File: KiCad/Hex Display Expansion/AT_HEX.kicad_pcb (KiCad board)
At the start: 2 copper layers, 101.1 x 77.4 mm, 38 parts, among them J1 Expansion Connector, J2 PWR, Q1 BC557, Q2 BC557, Q3 BC557, Q4 BC557, Q5 BC557, Q6 BC557, U1 NE555P, U10 HDSP-7801, U11 HDSP-7801, U12 HDSP-7801, U13 74HC244, U14 74HC244, U2 GAL16V8, U3 HDSP-7801, U4 HDSP-7801, U5 74HC74, U6 74HC00, U7 74HC04, U8 GAL16V8, U9 HDSP-7801

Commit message: Hex Display Updates WIP
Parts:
- removed the REF** at (111.7, 63.6)
- moved REF** 42.8 mm to (163.7, 112.2)
- moved REF** 17.3 mm to (157.3, 71.2), turned to 180 degrees
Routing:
- net /~Q0: track 26.6 -> 49.4 mm, vias 0 -> 1
- net /Q1: track 18.4 -> 31.6 mm, vias 0 -> 1
- net EN_H: track 110.7 -> 112.7 mm
- net HEX2: track 106.4 -> 107.8 mm
- net (no net): vias 1 -> 0
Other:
- board text added: "AT65C02 Hex Display"
- board text added: "https://github.com/Kayto"
- board text removed: "+3.3V"
- board text removed: "+5V"
- board text removed: "65C02 Hobby Computer - AT65C02"
- board text removed: "A00"
- board text removed: "A01"
- board text removed: "A02"
- board text removed: "A03"
- board text removed: "A04"
- board text removed: "A05"
- board text removed: "A06"
- board text removed: "A07"
- board text removed: "A08"
- board text removed: "A09"
- board text removed: "A10"
- board text removed: "A11"
- board text removed: "A12"
- board text removed: "A13"
- board text removed: "A14"
- board text removed: "A15"
- board text removed: "Based on Ben Eater’s 6502 project and"
- board text removed: "CLK"
- board text removed: "D0"
- board text removed: "D1"
- board text removed: "D2"
- board text removed: "D3"
- board text removed: "D4"
- board text removed: "D5"
- board text removed: "D6"
- board text removed: "D7"
- board text removed: "GND"
- board text removed: "NC"
- board text removed: "R~W"
- board text removed: "SIGNAL"
- board text removed: "https://github.com/dbuchwald/6502"
- board text removed: "the PCB designs by Dawid Buchwald"
- board text removed: "~IOCS"
- board text removed: "~IRQ"
- board text removed: "~RES"
- board text removed: "~ROMCS"
- board text removed: "~ROMOE"

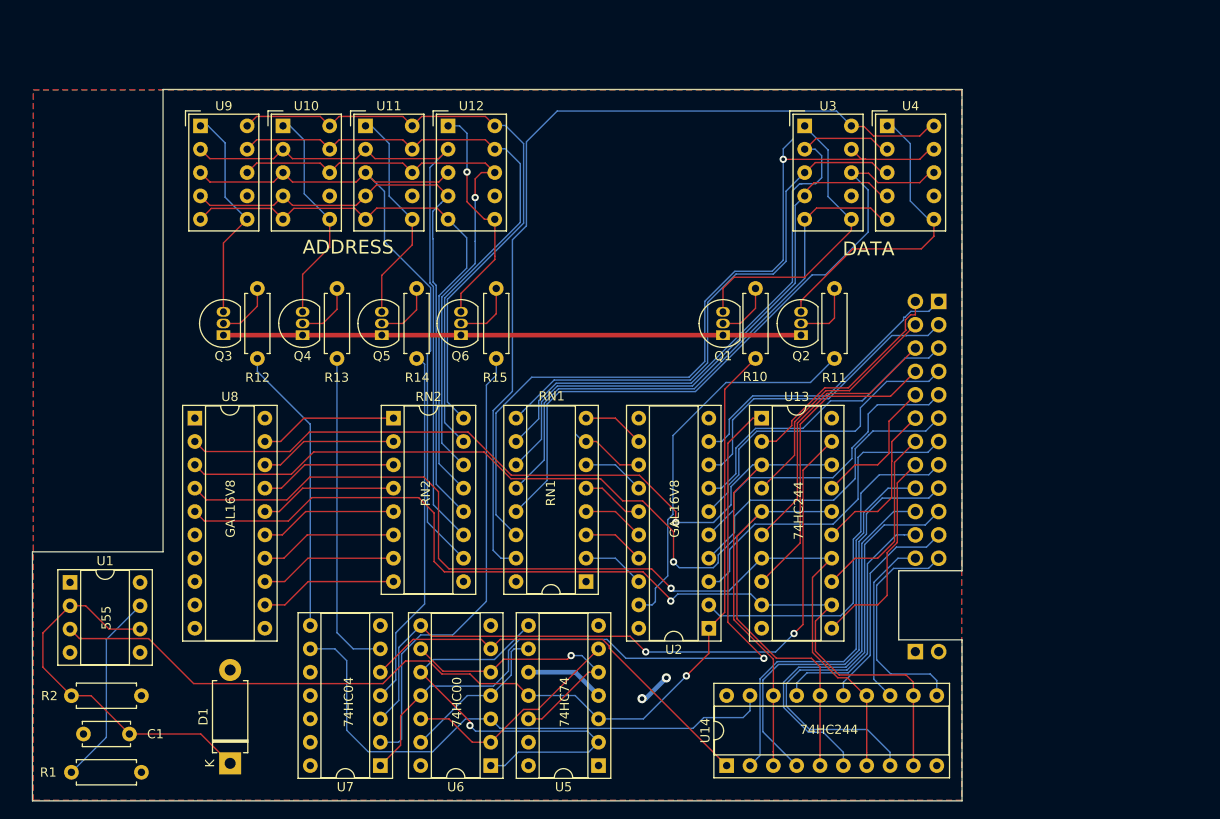
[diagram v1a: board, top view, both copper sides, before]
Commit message: HEX Board Mods
Hex board changes. Main board Hex to Latches
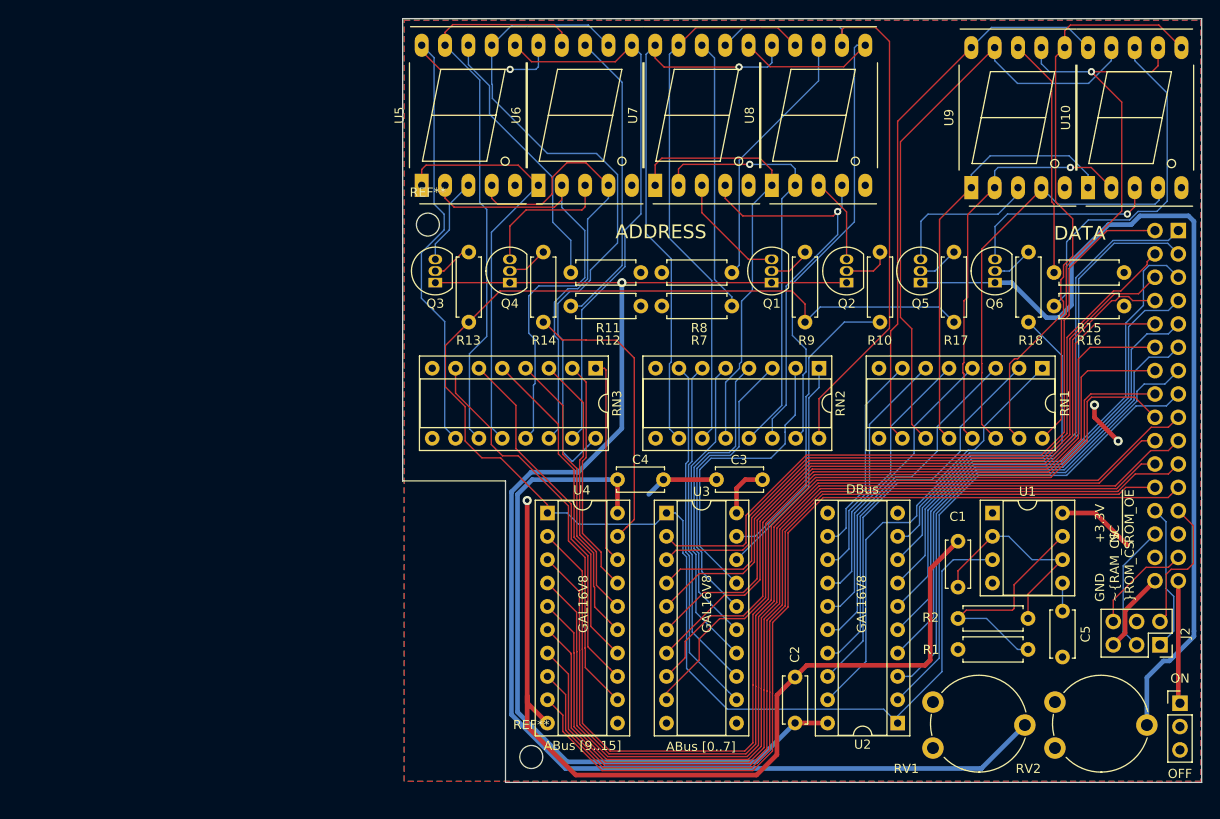
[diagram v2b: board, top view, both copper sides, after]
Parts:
- removed D1: D, Diode_THT:D_DO-15_P10.16mm_Horizontal
- removed U11, U12: HDSP-7801, Display_7Segment:HDSP-7801
- removed U13, U14: 74HC244, Package_DIP:DIP-20_W7.62mm_Socket
- added C2: 100n, Capacitor_THT:C_Disc_D5.0mm_W2.5mm_P5.00mm, F.Cu at (177.6, 113.5)
- added C3: 100n, Capacitor_THT:C_Disc_D5.0mm_W2.5mm_P5.00mm, F.Cu at (174.0, 87.0)
- added C4: 100n, Capacitor_THT:C_Disc_D5.0mm_W2.5mm_P5.00mm, F.Cu at (158.2, 87.0)
- added C5: 0.01uF, Capacitor_THT:C_Disc_D5.0mm_W2.5mm_P5.00mm, F.Cu at (206.7, 101.3)
- added J3: Conn_01x03, Connector_PinHeader_2.54mm:PinHeader_1x03_P2.54mm_Vertical, F.Cu at (219.4, 111.4)
- added R16: 2k2, Resistor_THT:R_Axial_DIN0207_L6.3mm_D2.5mm_P7.62mm_Horizontal, F.Cu at (205.7, 68.2)
- added R17: 4k7, Resistor_THT:R_Axial_DIN0207_L6.3mm_D2.5mm_P7.62mm_Horizontal, F.Cu at (194.9, 62.3)
- added R18: 2k2, Resistor_THT:R_Axial_DIN0207_L6.3mm_D2.5mm_P7.62mm_Horizontal, F.Cu at (203.0, 62.3)
- added R7: 4k7, Resistor_THT:R_Axial_DIN0207_L6.3mm_D2.5mm_P7.62mm_Horizontal, F.Cu at (163.1, 68.2)
- added R8: 4k7, Resistor_THT:R_Axial_DIN0207_L6.3mm_D2.5mm_P7.62mm_Horizontal, F.Cu at (163.1, 64.5)
- added R9: 4k7, Resistor_THT:R_Axial_DIN0207_L6.3mm_D2.5mm_P7.62mm_Horizontal, F.Cu at (178.6, 62.3)
- added REF**: MountingHole_2.5mm, MountingHole:MountingHole_2.5mm, F.Cu at (148.9, 117.2)
- added REF**: MountingHole_2.5mm, MountingHole:MountingHole_2.5mm, F.Cu at (137.6, 59.3)
- added RN3: 100, Package_DIP:DIP-16_W7.62mm_Socket, F.Cu at (155.9, 74.9)
- added RV1: R_POT_Small, Potentiometer_THT:Potentiometer_Piher_PT-10-V10_Vertical, F.Cu at (192.6, 116.2)
- added RV2: R_POT_Small, Potentiometer_THT:Potentiometer_Piher_PT-10-V10_Vertical, F.Cu at (205.8, 116.2)
- C1: value 68n -> 0.01uF
- J1: footprint Connector_PinHeader_2.54mm:PinHeader_2x12_P2.54mm_Vertical -> Connector_PinHeader_2.54mm:PinHeader_2x16_P2.54mm_Vertical
- J2: value PWR -> Conn_02x03_Odd_Even; footprint Connector_PinHeader_2.54mm:PinHeader_1x02_P2.54mm_Vertical -> Connector_PinSocket_2.54mm:PinSocket_2x03_P2.54mm_Vertical; moved to F.Cu
- R1: value 51k -> 1k
- R11, R12, R13, R14: value 2k2 -> 4k7
- R2: value 51k -> 100k
- U10, U9: value HDSP-7801 -> E10561; footprint Display_7Segment:HDSP-7801 -> Display_7Segment:7SegmentLED_LTS6760_LTS6780
- U3, U4: value HDSP-7801 -> GAL16V8; footprint Display_7Segment:HDSP-7801 -> Package_DIP:DIP-20_W7.62mm_Socket
- U5: value 74HC74 -> E10561; footprint Package_DIP:DIP-14_W7.62mm_Socket -> Display_7Segment:7SegmentLED_LTS6760_LTS6780
- U6: value 74HC00 -> E10561; footprint Package_DIP:DIP-14_W7.62mm_Socket -> Display_7Segment:7SegmentLED_LTS6760_LTS6780
- U7: value 74HC04 -> E10561; footprint Package_DIP:DIP-14_W7.62mm_Socket -> Display_7Segment:7SegmentLED_LTS6760_LTS6780
- U8: value GAL16V8 -> E10561; footprint Package_DIP:DIP-20_W7.62mm_Socket -> Display_7Segment:7SegmentLED_LTS6760_LTS6780
- moved U1 100.6 mm to (199.0, 90.7)
- moved C1 91.6 mm to (195.3, 98.8), turned to 90 degrees
- moved R1 89.8 mm to (195.3, 105.5), turned to 0 degrees
- moved R2 89.2 mm to (195.3, 102.2), turned to 0 degrees
- moved U10 87.8 mm to (209.4, 55.3), turned to 90 degrees
- moved U9 84.1 mm to (196.7, 55.3), turned to 90 degrees
- moved REF** 71.3 mm to (191.0, 46.3)
- moved U7 69.9 mm to (162.3, 55.0), turned to 90 degrees
- moved U8 67.7 mm to (175.0, 55.0), turned to 90 degrees
- moved U5 66.0 mm to (136.9, 55.0), turned to 90 degrees
- moved U6 63.3 mm to (149.6, 55.0), turned to 90 degrees
- moved R15 60.7 mm to (205.7, 64.5), turned to 0 degrees
- moved Q5 58.9 mm to (191.2, 65.6)
- moved Q6 58.4 mm to (199.3, 65.6)
- moved U4 56.0 mm to (150.6, 90.7)
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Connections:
- J2 pad 1: +5V -> ~ROM_CS
- J2 pad 2: GND -> ~ROM_OE
- Q1 pad 1: +5V -> Net-(Q1-Pad1)
- Q2 pad 1: +5V -> Net-(Q1-Pad1)
- Q3 pad 1: +5V -> Net-(Q1-Pad1)
- Q4 pad 1: +5V -> Net-(Q1-Pad1)
- Q5 pad 1: +5V -> Net-(Q5-Pad1)
- Q6 pad 1: +5V -> Net-(Q5-Pad1)
- R10 pad 1: Net-(Q1-Pad2) -> Net-(Q2-Pad2)
- R10 pad 2: EN_H -> EN_a0L
- R11 pad 1: Net-(Q2-Pad2) -> GND
- R11 pad 2: EN_D0 -> Net-(R11-Pad2)
- R12 pad 1: Net-(Q3-Pad2) -> GND
- R13 pad 1: Net-(Q4-Pad2) -> Net-(Q3-Pad2)
- R13 pad 2: Net-(R13-Pad2) -> EN_H
- R14 pad 1: Net-(Q5-Pad2) -> Net-(Q4-Pad2)
- R14 pad 2: Net-(R14-Pad2) -> EN_a8L
- R15 pad 1: Net-(Q6-Pad2) -> Net-(R15-Pad1)
- R15 pad 2: Net-(R15-Pad2) -> GND
- R2 pad 1: +5V -> Net-(R1-Pad2)
- RN2 pad 10: /16 bit Hex/G -> Net-(RN2-Pad10)
- RN2 pad 11: /16 bit Hex/F -> Net-(RN2-Pad11)
- RN2 pad 12: /16 bit Hex/E -> Net-(RN2-Pad12)
- RN2 pad 13: /16 bit Hex/D -> Net-(RN2-Pad13)
- RN2 pad 14: /16 bit Hex/C -> Net-(RN2-Pad14)
- RN2 pad 15: /16 bit Hex/B -> Net-(RN2-Pad15)
- RN2 pad 16: /16 bit Hex/A -> Net-(RN2-Pad16)
- U1 pad 4: +5V -> Net-(U1-Pad4)
- U10 pad 1: Net-(Q4-Pad3) -> Net-(RN1-Pad12)
- U10 pad 10: /16 bit Hex/A -> Net-(RN1-Pad10)
- U10 pad 2: /16 bit Hex/F -> Net-(RN1-Pad13)
- U10 pad 3: /16 bit Hex/G -> Net-(Q6-Pad3)
- U10 pad 4: /16 bit Hex/E -> Net-(RN1-Pad14)
- U10 pad 5: /16 bit Hex/D -> Net-(U10-Pad5)
- U10 pad 6: Net-(Q4-Pad3) -> Net-(RN1-Pad15)
- U10 pad 7: Net-(U10-Pad7) -> Net-(RN1-Pad16)
- U10 pad 8: /16 bit Hex/C -> Net-(R16-Pad1)
- U10 pad 9: /16 bit Hex/B -> Net-(RN1-Pad11)
- U2 pad 10: GND -> Net-(U2-Pad10)
- U2 pad 12: Net-(RN1-Pad8) -> Net-(RN1-Pad7)
- U2 pad 13: Net-(RN1-Pad7) -> Net-(RN1-Pad6)
- U2 pad 14: Net-(RN1-Pad6) -> Net-(RN1-Pad5)
- U2 pad 15: Net-(RN1-Pad5) -> Net-(RN1-Pad4)
- U2 pad 16: Net-(RN1-Pad4) -> Net-(RN1-Pad3)
- U2 pad 17: Net-(RN1-Pad3) -> Net-(RN1-Pad2)
- U2 pad 18: Net-(RN1-Pad2) -> Net-(RN1-Pad1)
- U2 pad 19: EN_D0 -> EN_DL
- U3 pad 1: Net-(Q1-Pad3) -> EN_H
- U3 pad 10: Net-(RN1-Pad15) -> GND
- U3 pad 2: Net-(RN1-Pad10) -> a0
- U3 pad 3: Net-(RN1-Pad9) -> a1
- U3 pad 4: Net-(RN1-Pad11) -> a2
- U3 pad 5: Net-(RN1-Pad12) -> a3
- U3 pad 6: Net-(Q1-Pad3) -> a4
- U3 pad 7: Net-(U3-Pad7) -> a5
- U3 pad 8: Net-(RN1-Pad13) -> a6
- U3 pad 9: Net-(RN1-Pad14) -> a7
- U4 pad 1: Net-(Q2-Pad3) -> EN_H
- U4 pad 10: Net-(RN1-Pad15) -> GND
- U4 pad 2: Net-(RN1-Pad10) -> a8
- U4 pad 3: Net-(RN1-Pad9) -> a9
- U4 pad 4: Net-(RN1-Pad11) -> a10
- U4 pad 5: Net-(RN1-Pad12) -> a11
- U4 pad 6: Net-(Q2-Pad3) -> a12
- U4 pad 7: Net-(U4-Pad7) -> a13
- U4 pad 8: Net-(RN1-Pad13) -> a14
- U4 pad 9: Net-(RN1-Pad14) -> a15
- U5 pad 1: +5V -> Net-(RN3-Pad12)
- U5 pad 10: +5V -> Net-(RN3-Pad10)
- U5 pad 2: /~Q0 -> Net-(RN3-Pad13)
- U5 pad 3: EN_H -> Net-(Q3-Pad3)
- U5 pad 4: +5V -> Net-(RN3-Pad14)
- U5 pad 5: /Q1 -> Net-(U5-Pad5)
- U5 pad 6: /~Q1 -> Net-(RN3-Pad15)
- U5 pad 7: GND -> Net-(RN3-Pad16)
- U5 pad 8: /~Q0 -> Net-(R11-Pad2)
- U5 pad 9: /Q0 -> Net-(RN3-Pad11)
- U6 pad 1: /~Q0 -> Net-(RN3-Pad12)
- U6 pad 10: /~Q0 -> Net-(RN3-Pad10)
- U6 pad 2: /~Q1 -> Net-(RN3-Pad13)
- U6 pad 3: EN_DIG0 -> Net-(Q4-Pad3)
- U6 pad 4: /Q0 -> Net-(RN3-Pad14)
- U6 pad 5: /Q1 -> Net-(U6-Pad5)
- U6 pad 6: EN_DIG1 -> Net-(RN3-Pad15)
- U6 pad 7: GND -> Net-(RN3-Pad16)
- U6 pad 8: EN_DIG2 -> Net-(R12-Pad2)
- U6 pad 9: /Q1 -> Net-(RN3-Pad11)
- U7 pad 1: EN_DIG3 -> Net-(RN2-Pad12)
- U7 pad 10: (no net) -> Net-(RN2-Pad10)
- U7 pad 2: Net-(R15-Pad2) -> Net-(RN2-Pad13)
- U7 pad 3: EN_DIG2 -> Net-(Q1-Pad3)
- U7 pad 4: Net-(R14-Pad2) -> Net-(RN2-Pad14)
- U7 pad 5: EN_DIG1 -> Net-(U7-Pad5)
- U7 pad 6: Net-(R13-Pad2) -> Net-(RN2-Pad15)
- U7 pad 7: GND -> Net-(RN2-Pad16)
- U7 pad 8: Net-(R12-Pad2) -> Net-(R7-Pad2)
- U7 pad 9: EN_DIG0 -> Net-(RN2-Pad11)
- U8 pad 1: Net-(U8-Pad1) -> Net-(RN2-Pad12)
- U8 pad 10: GND -> Net-(RN2-Pad10)
- U8 pad 2: HEX0 -> Net-(RN2-Pad13)
- U8 pad 3: HEX1 -> Net-(Q2-Pad3)
- U8 pad 4: HEX2 -> Net-(RN2-Pad14)
- U8 pad 5: HEX3 -> Net-(U8-Pad5)
- U8 pad 6: Net-(U8-Pad6) -> Net-(RN2-Pad15)
- U8 pad 7: Net-(U8-Pad7) -> Net-(RN2-Pad16)
- U8 pad 9: Net-(U8-Pad9) -> Net-(RN2-Pad11)
- U9 pad 1: Net-(Q3-Pad3) -> Net-(RN1-Pad12)
- U9 pad 10: /16 bit Hex/A -> Net-(RN1-Pad10)
- U9 pad 2: /16 bit Hex/F -> Net-(RN1-Pad13)
- U9 pad 3: /16 bit Hex/G -> Net-(Q5-Pad3)
- U9 pad 4: /16 bit Hex/E -> Net-(RN1-Pad14)
- U9 pad 5: /16 bit Hex/D -> Net-(U9-Pad5)
- U9 pad 6: Net-(Q3-Pad3) -> Net-(RN1-Pad15)
- U9 pad 7: Net-(U9-Pad7) -> Net-(RN1-Pad16)
- U9 pad 8: /16 bit Hex/C -> Net-(R15-Pad1)
- U9 pad 9: /16 bit Hex/B -> Net-(RN1-Pad11)
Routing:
- net Net-(Q1-Pad1): track 0.00 -> 160.0 mm, vias 0 -> 1
- net GND: track 0.00 -> 120.0 mm, vias 0 -> 3
- net HEX1: track 115.2 -> 0.00 mm, vias 1 -> 0
- net HEX0: track 115.0 -> 0.00 mm, vias 1 -> 0
- net HEX2: track 107.8 -> 0.00 mm, vias 1 -> 0
- net HEX3: track 106.3 -> 0.00 mm, vias 1 -> 0
- net Net-(Q5-Pad1): track 0.00 -> 96.2 mm
- net EN_DIG3: track 81.4 -> 0.00 mm, vias 1 -> 0
- net a13: track 23.7 -> 103.7 mm
- net a14: track 18.6 -> 98.1 mm
- net EN_DIG2: track 77.2 -> 0.00 mm, vias 2 -> 0
- net a12: track 26.7 -> 103.2 mm
- net /16 bit Hex/G: track 76.2 -> 0.00 mm
- net Net-(RN3-Pad16): track 0.00 -> 76.1 mm
- net a8: track 43.6 -> 117.8 mm
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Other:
- board size 101.1 x 77.4 mm -> 86.9 x 83.1 mm
- board text added: "+3.3V NC ~ROM_OE"
- board text added: "ABus [0..7]"
- board text added: "ABus [9..15]"
- board text added: "DBus"
- board text added: "GND ~RAM_CS ~ROM_CS"
- board text added: "OFF"
- board text added: "ON"
- board text removed: "555"
- board text removed: "74HC00"
- board text removed: "74HC04"
- board text removed: "74HC244"
- board text removed: "74HC74"
- board text removed: "RN1"
- board text removed: "RN2"
- board text removed: "https://github.com/kayto/AT65C02"

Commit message: release revisions
REv001,002 and HEX
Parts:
- REF**: value MountingHole_2.5mm -> MountingHole_2.1mm; footprint MountingHole:MountingHole_2.5mm -> MountingHole:MountingHole_2.1mm
- moved REF** 17.3 mm to (160.9, 104.8)
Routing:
- net GND: track 120.0 -> 124.2 mm
- net +5V: track 91.1 -> 92.8 mm
- net Net-(Q1-Pad1): track 160.0 -> 161.8 mm
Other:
- board text added: "+3.3V NC ~ROMOE"
- board text added: "ABus [8..15]"
- board text added: "GND ~RAMCS ~ROMCS"
- board text removed: "+3.3V NC ~ROM_OE"
- board text removed: "ABus [9..15]"
- board text removed: "GND ~RAM_CS ~ROM_CS"
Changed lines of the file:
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@@
     (thickness 1.6)
     (drawings 23)
-    (tracks 991)
+    (tracks 993)
     (zones 0)
     (modules 48)
@@
   (page A4)
   (layers
-    (0 F.Cu signal)
-    (31 B.Cu signal)
+    (0 F.Cu signal hide)
+    (31 B.Cu signal hide)
     (32 B.Adhes user)
     (33 F.Adhes user)
     (34 B.Paste user)
     (35 F.Paste user)
-    (36 B.SilkS user hide)
+    (36 B.SilkS user)
     (37 F.SilkS user)
     (38 B.Mask user)
@@
   )
   (setup
-    (last_trace_width 0.508)
+    (last_trace_width 0.1524)
     (user_trace_width 0.25)
     (user_trace_width 0.25)
@@
       (drillshape 0)
       (scaleselection 1)
-      (outputdirectory "Gerbers/AT_65c02/"))
+      (outputdirectory "../../Gerbers/Hex Rev001/"))
   )
   (net 0 "")
@@
     (add_net GND)
   )
-  (module MountingHole:MountingHole_2.5mm (layer F.Cu)
-    (at 148.865 117.225)
-    (descr "Mounting Hole 2.5mm, no annular")
-    (tags "mounting hole 2.5mm no annular")
+  (module MountingHole:MountingHole_2.1mm (layer F.Cu)
+    (at 160.89 104.775)
+    (descr "Mounting Hole 2.1mm, no annular")
+    (tags "mounting hole 2.1mm no annular")
     (attr virtual)
-    (fp_text reference REF** (at 0 -3.5) (layer F.SilkS)
+    (fp_text reference REF** (at 0 -3.5) (layer F.SilkS) hide
       (effects (font (size 1 1) (thickness 0.15)))
     )
-    (fp_text value MountingHole_2.5mm (at 0 3.5) (layer F.Fab)
+    (fp_text value MountingHole_2.1mm (at 0 3.5) (layer F.Fab)
       (effects (font (size 1 1) (thickness 0.15)))
     )
-    (fp_circle (center 0 0) (end 2.75 0) (layer F.CrtYd) (width 0.05))
-    (fp_circle (center 0 0) (end 2.5 0) (layer Cmts.User) (width 0.15))
+    (fp_circle (center 0 0) (end 2.35 0) (layer F.CrtYd) (width 0.05))
+    (fp_circle (center 0 0) (end 2.1 0) (layer Cmts.User) (width 0.15))
     (fp_text user %R (at 0.3 0) (layer F.Fab)
       (effects (font (size 1 1) (thickness 0.15)))
     )
-    (pad 1 np_thru_hole circle (at 0 0) (size 2.5 2.5) (drill 2.5) (layers *.Cu *.Mask))
+    (pad "" np_thru_hole circle (at 0 0) (size 2.1 2.1) (drill 2.1) (layers *.Cu *.Mask))
   )
   (module MountingHole:MountingHole_2.5mm (layer F.Cu)
@@
     (tags "mounting hole 2.5mm no annular")
     (attr virtual)
-    (fp_text reference REF** (at 0 -3.5) (layer F.SilkS)
+    (fp_text reference REF** (at 0 -3.5) (layer F.SilkS) hide
       (effects (font (size 1 1) (thickness 0.15)))
     )
@@
     (descr "7-Segment Display, LTS67x0, http://optoelectronics.liteon.com/upload/download/DS30-2001-355/S6760jd.pdf")
     (tags "7Segment LED LTS6760 LTS6780")
-    (fp_text reference U5 (at 7.62 -2.42 90) (layer F.SilkS)
+    (fp_text reference U5 (at 7.903 -0.225 90) (layer F.SilkS)
       (effects (font (size 1 1) (thickness 0.15)))
     )
@@
       (effects (font (size 1 1) (thickness 0.15)))
     )
-    (fp_text user %R (at 0 2.54 90) (layer F.Fab)
-      (effects (font (size 1 1) (thickness 0.15)))
-    )
     (fp_line (start -0.635 -1.27) (end 1.27 -1.27) (layer F.Fab) (width 0.1))
     (fp_line (start 1.27 -1.27) (end 1.27 6.35) (layer F.Fab) (width 0.1))
@@
     (fp_line (start 1.8 6.85) (end 1.8 -1.8) (layer F.CrtYd) (width 0.05))
     (fp_line (start 1.8 -1.8) (end -1.8 -1.8) (layer F.CrtYd) (width 0.05))
+    (fp_text user %R (at 0 2.54 90) (layer F.Fab)
+      (effects (font (size 1 1) (thickness 0.15)))
+    )
     (pad 3 thru_hole oval (at 0 5.08) (size 1.7 1.7) (drill 1) (layers *.Cu *.Mask)
       (net 122 "Net-(J3-Pad3)"))
@@
     (effects (font (size 1 1) (thickness 0.15)))
   )
-  (gr_text "GND\n~RAM_CS\n~ROM_CS" (at 212.34 100.35 90) (layer F.SilkS)
+  (gr_text "GND\n~RAMCS\n~ROMCS" (at 212.34 100.35 90) (layer F.SilkS)
     (effects (font (size 1 1) (thickness 0.15)) (justify left))
   )
@@
     (effects (font (size 1 1) (thickness 0.15)))
   )
-  (gr_text "ABus [9..15]" (at 154.44 116) (layer F.SilkS)
+  (gr_text "ABus [8..15]" (at 154.44 116) (layer F.SilkS)
     (effects (font (size 1 1) (thickness 0.15)))
   )
@@
     (effects (font (size 1 1) (thickness 0.15)))
   )
-  (gr_text "+3.3V\nNC\n~ROM_OE" (at 212.34 93.95 90) (layer F.SilkS)
+  (gr_text "+3.3V\nNC\n~ROMOE" (at 212.34 94.55 90) (layer F.SilkS)
     (effects (font (size 1 1) (thickness 0.15)) (justify left))
   )
@@
   (segment (start 210.14 80.275) (end 212.715 82.85) (width 0.508) (layer F.Cu) (net 2))
   (segment (start 210.14 78.925) (end 210.14 80.275) (width 0.508) (layer F.Cu) (net 2))
-  (segment (start 153.706287 119.191287) (end 148.415 113.9) (width 0.508) (layer F.Cu) (net 2))
-  (segment (start 173.373713 119.191287) (end 153.706287 119.191287) (width 0.508) (layer F.Cu) (net 2))
+  (segment (start 147.34 90.4) (end 148.415 89.325) (width 0.508) (layer F.Cu) (net 2))
+  (segment (start 147.34 109.5) (end 147.34 90.4) (width 0.508) (layer F.Cu) (net 2))
+  (segment (start 147.34 110.256) (end 147.34 109.5) (width 0.508) (layer F.Cu) (net 2))
+  (segment (start 150.622 113.538) (end 147.34 110.256) (width 0.508) (layer F.Cu) (net 2))
+  (segment (start 147.34 111.3) (end 147.34 109.5) (width 0.508) (layer F.Cu) (net 2))
+  (segment (start 147.34 115.85) (end 147.34 111.3) (width 0.508) (layer F.Cu) (net 2))
+  (segment (start 150.681287 119.191287) (end 147.34 115.85) (width 0.508) (layer F.Cu) (net 2))
+  (segment (start 173.373713 119.191287) (end 150.681287 119.191287) (width 0.508) (layer F.Cu) (net 2))
   (segment (start 175.59 116.975) (end 173.373713 119.191287) (width 0.508) (layer F.Cu) (net 2))
   (segment (start 175.59 110.5) (end 175.59 116.975) (width 0.508) (layer F.Cu) (net 2))
   (segment (start 177.565 108.525) (end 175.59 110.5) (width 0.508) (layer F.Cu) (net 2))
-  (segment (start 148.415 111.331) (end 148.415 110.575) (width 0.508) (layer F.Cu) (net 2))
-  (segment (start 150.622 113.538) (end 148.415 111.331) (width 0.508) (layer F.Cu) (net 2))
-  (segment (start 148.415 110.575) (end 148.415 89.325) (width 0.508) (layer F.Cu) (net 2))
-  (segment (start 148.415 113.9) (end 148.415 110.575) (width 0.508) (layer F.Cu) (net 2))
   (segment (start 174.015 87.05) (end 172.14 87.05) (width 0.508) (layer F.Cu) (net 3))
   (segment (start 171.196 87.994) (end 171.196 90.678) (width 0.508) (layer F.Cu) (net 3))
@@
   (segment (start 213.766401 94.226401) (end 210.218 90.678) (width 0.508) (layer F.Cu) (net 3))
   (segment (start 157.11063 87.05) (end 158.242 87.05) (width 0.508) (layer B.Cu) (net 3))
-  (segment (start 147.365 88.65) (end 148.965 87.05) (width 0.508) (layer B.Cu) (net 3))
-  (segment (start 147.365 112.341038) (end 147.365 88.65) (width 0.508) (layer B.Cu) (net 3))
   (segment (start 148.965 87.05) (end 157.11063 87.05) (width 0.508) (layer B.Cu) (net 3))
-  (segment (start 173.34 117.75) (end 152.773962 117.75) (width 0.508) (layer B.Cu) (net 3))
+  (segment (start 147.365 115.3) (end 147.365 88.65) (width 0.508) (layer B.Cu) (net 3))
+  (segment (start 147.365 88.65) (end 148.965 87.05) (width 0.508) (layer B.Cu) (net 3))
   (segment (start 177.565 113.525) (end 173.34 117.75) (width 0.508) (layer B.Cu) (net 3))
-  (segment (start 152.773962 117.75) (end 147.365 112.341038) (width 0.508) (layer B.Cu) (net 3))
+  (segment (start 149.815 117.75) (end 147.365 115.3) (width 0.508) (layer B.Cu) (net 3))
+  (segment (start 173.34 117.75) (end 149.815 117.75) (width 0.508) (layer B.Cu) (net 3))
   (segment (start 172.49 63.08) (end 175.006 63.08) (width 0.1524) (layer F.Cu) (net 4))
   (segment (start 167.42 58.01) (end 172.49 63.08) (width 0.1524) (layer F.Cu) (net 4))
@@
   (via (at 158.72 65.62) (size 1) (drill 0.508) (layers F.Cu B.Cu) (net 111))
   (segment (start 197.84 118.475) (end 202.565 113.75) (width 0.508) (layer B.Cu) (net 111))
-  (segment (start 197.815 118.475) (end 197.89 118.4) (width 0.508) (layer B.Cu) (net 111))
-  (segment (start 146.704589 112.614589) (end 152.565 118.475) (width 0.508) (layer B.Cu) (net 111))
-  (segment (start 146.704589 88.376449) (end 146.704589 112.614589) (width 0.508) (layer B.Cu) (net 111))
-  (segment (start 152.565 118.475) (end 197.815 118.475) (width 0.508) (layer B.Cu) (net 111))
-  (segment (start 148.841449 86.239589) (end 146.704589 88.376449) (width 0.508) (layer B.Cu) (net 111))
+  (segment (start 149.606038 118.475) (end 197.815 118.475) (width 0.508) (layer B.Cu) (net 111))
+  (segment (start 146.704589 115.573551) (end 149.606038 118.475) (width 0.508) (layer B.Cu) (net 111))
+  (segment (start 146.704589 88.376449) (end 146.704589 115.573551) (width 0.508) (layer B.Cu) (net 111))
   (segment (start 153.959885 86.239589) (end 148.841449 86.239589) (width 0.508) (layer B.Cu) (net 111))
-  (segment (start 158.72 81.479474) (end 153.959885 86.239589) (width 0.508) (layer B.Cu) (net 111))
   (segment (start 158.72 65.62) (end 158.72 81.479474) (width 0.508) (layer B.Cu) (net 111))
+  (segment (start 158.72 81.479474) (end 153.959885 86.239589) (width 0.508) (layer B.Cu) (net 111))
+  (segment (start 197.815 118.475) (end 197.89 118.4) (width 0.508) (layer B.Cu) (net 111))
+  (segment (start 148.841449 86.239589) (end 146.704589 88.376449) (width 0.508) (layer B.Cu) (net 111))
   (segment (start 191.210666 65.62) (end 199.316 65.62) (width 0.1524) (layer B.Cu) (net 112))
   (segment (start 220.365 58.35) (end 220.965 58.95) (width 0.508) (layer B.Cu) (net 112))
